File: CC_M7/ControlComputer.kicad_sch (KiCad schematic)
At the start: 41 parts, among them J1 1x03_BootPin, U1 STM32H743VITx, Y1 25MHz

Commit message: update
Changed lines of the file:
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@@
 	(wire
 		(pts
-			(xy 104.14 140.97) (xy 113.03 140.97)
+			(xy 104.14 140.97) (xy 118.11 140.97)
 		)
 		(stroke
@@
 	(global_label "ADC1"
 		(shape input)
-		(at 113.03 140.97 0)
-		(fields_autoplaced yes)
-		(effects
-			(font
-				(size 1.27 1.27)
-			)
-			(justify left)
-		)
-		(property "Intersheetrefs" "${INTERSHEET_REFS}"
-			(at 120.8533 140.97 0)
-			(effects
-				(font
+		(at 118.11 140.97 0)
+		(fields_autoplaced yes)
+		(effects
+			(font
+				(size 1.27 1.27)
+			)
+			(justify left)
+		)
+		(property "Intersheetrefs" "${INTERSHEET_REFS}"
+			(at 125.9333 140.97 0)
+			(effects
+				(font

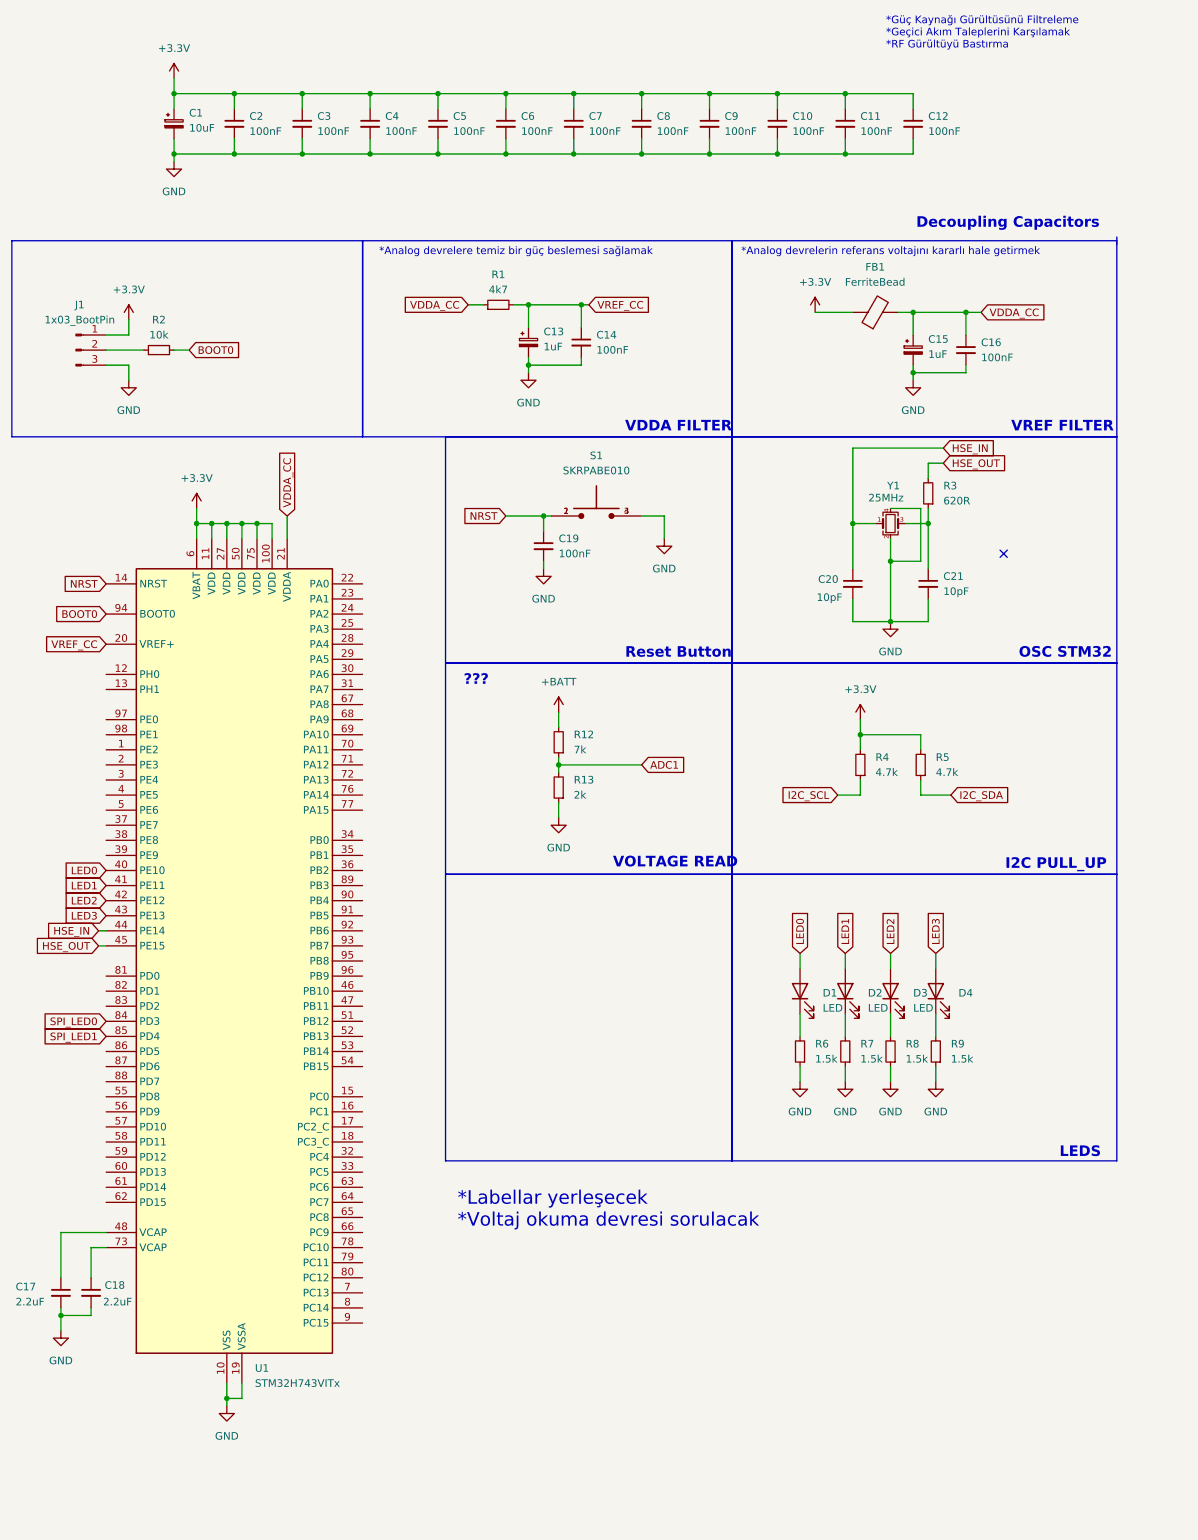
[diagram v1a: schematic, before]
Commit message: STM32H743VIT6 labels updated
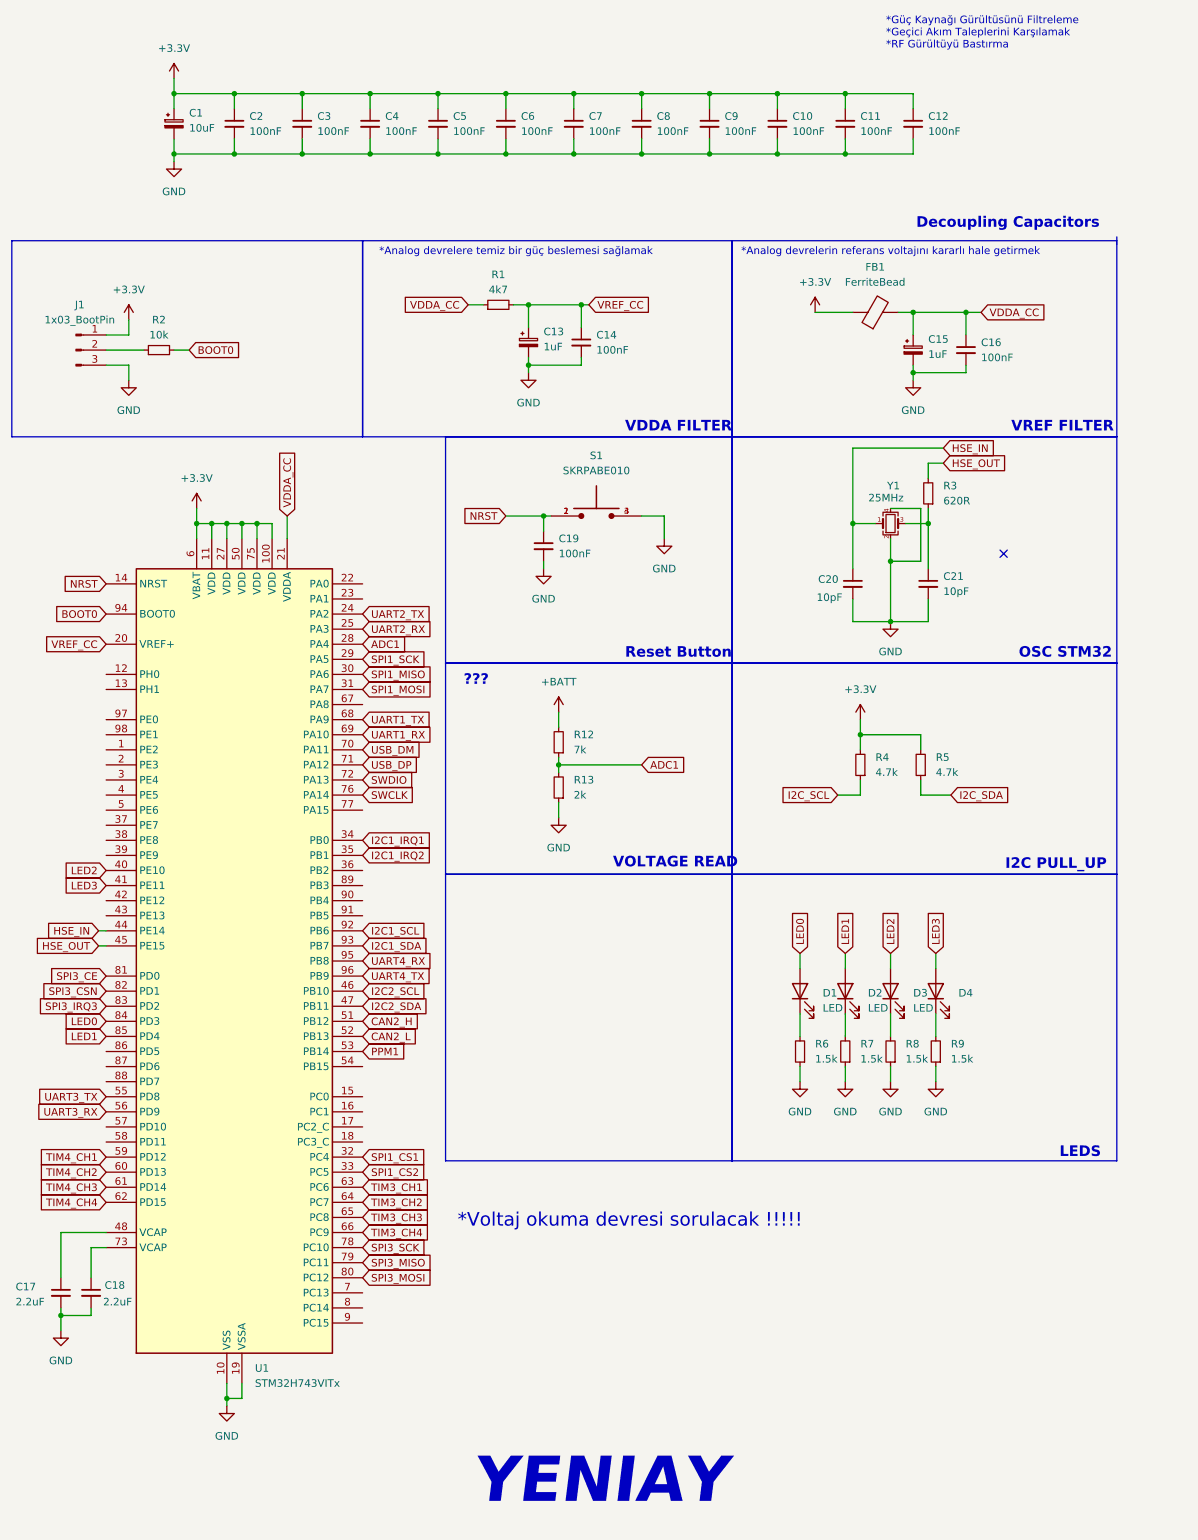
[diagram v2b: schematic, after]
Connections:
- net  SPI_LED0 is gone; now on net LED0: U1.84 (PD3)
- net SPI_LED1 is gone; now on net LED1: U1.85 (PD4)
- net ADC1: now also U1.28 (PA4)
- net LED0: no longer U1.40 (PE10)
- net LED1: no longer U1.41 (PE11)
- net LED2: now also U1.40 (PE10); no longer U1.42 (PE12)
- net LED3: now also U1.41 (PE11); no longer U1.43 (PE13)
- net UART2_TX: now reaches U1.24 (PA2)
- net UART2_RX: now reaches U1.25 (PA3)
- net SPI1_SCK: now reaches U1.29 (PA5)
- net SPI1_MISO: now reaches U1.30 (PA6)
- net SPI1_MOSI: now reaches U1.31 (PA7)
- net SPI1_CS1: now reaches U1.32 (PC4)
- net SPI1_CS2: now reaches U1.33 (PC5)
- net I2C1_IRQ1: now reaches U1.34 (PB0)
- net I2C1_IRQ2: now reaches U1.35 (PB1)
- net I2C2_SCL: now reaches U1.46 (PB10)
- net I2C2_SDA: now reaches U1.47 (PB11)
- net CAN2_H: now reaches U1.51 (PB12)
- net CAN2_L: now reaches U1.52 (PB13)
- net PPM1: now reaches U1.53 (PB14)
- net UART3_TX : now reaches U1.55 (PD8)
- net UART3_RX: now reaches U1.56 (PD9)
- net TIM4_CH1: now reaches U1.59 (PD12)
- net TIM4_CH2: now reaches U1.60 (PD13)
- net TIM4_CH3: now reaches U1.61 (PD14)
- net TIM4_CH4: now reaches U1.62 (PD15)
- net TIM3_CH1: now reaches U1.63 (PC6)
- net TIM3_CH2: now reaches U1.64 (PC7)
- net TIM3_CH3: now reaches U1.65 (PC8)
- net TIM3_CH4: now reaches U1.66 (PC9)
- net UART1_TX: now reaches U1.68 (PA9)
- net UART1_RX: now reaches U1.69 (PA10)
- net USB_DM: now reaches U1.70 (PA11)
- net USB_DP: now reaches U1.71 (PA12)
- net SWDIO: now reaches U1.72 (PA13)
- net SWCLK: now reaches U1.76 (PA14)
- net SPI3_SCK: now reaches U1.78 (PC10)
- net SPI3_MISO: now reaches U1.79 (PC11)
- net SPI3_MOSI: now reaches U1.80 (PC12)
- net SPI3_CE: now reaches U1.81 (PD0)
- net SPI3_CSN: now reaches U1.82 (PD1)
- net SPI3_IRQ3: now reaches U1.83 (PD2)
- net I2C1_SCL: now reaches U1.92 (PB6)
- net I2C1_SDA : now reaches U1.93 (PB7)
- net UART4_RX: now reaches U1.95 (PB8)
- net UART4_TX: now reaches U1.96 (PB9)
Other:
- note added: "*Voltaj okuma devresi sorulacak !!!!!"
- note added: "YENIAY"
- note removed: "*Labellar yerleşecek *Voltaj okuma devresi sorulacak"
- company: YENIAY -> (none)

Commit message: label control
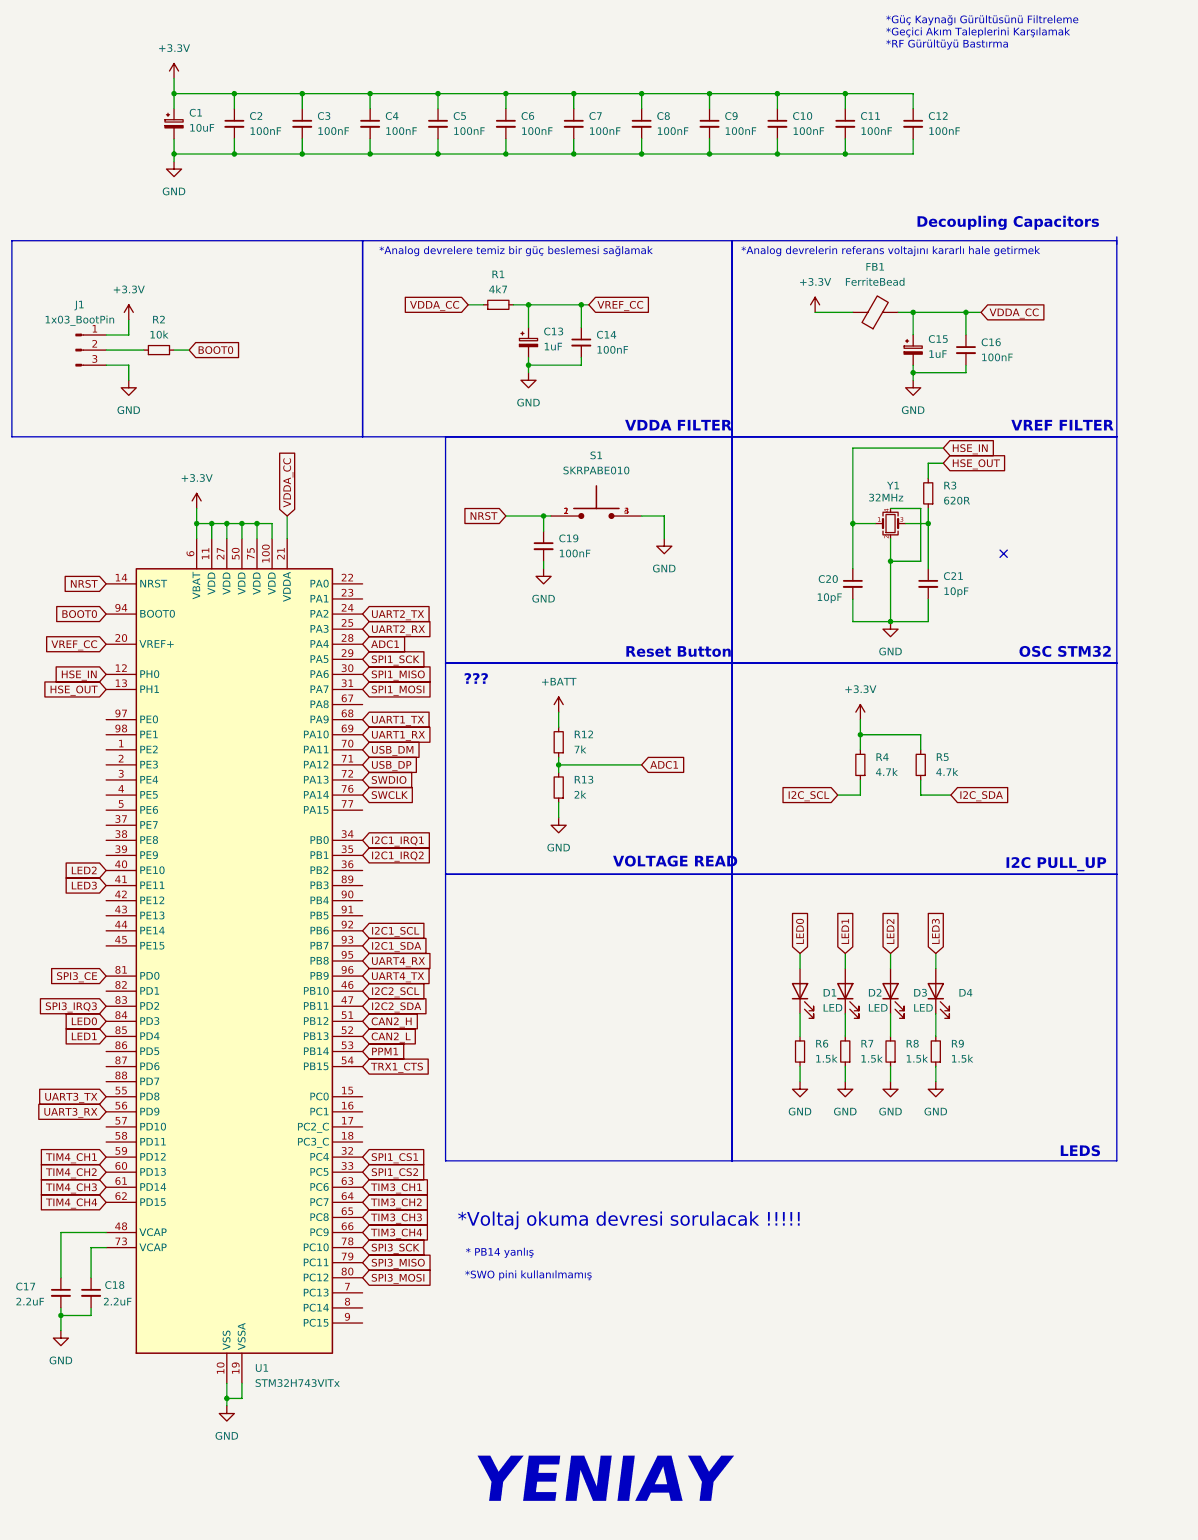
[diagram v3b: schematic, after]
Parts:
- Y1: value 25MHz -> 32MHz
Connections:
- net HSE_IN: now also U1.12 (PH0); no longer U1.44 (PE14)
- net HSE_OUT: now also U1.13 (PH1); no longer U1.45 (PE15)
- net TRX1_CTS: now reaches U1.54 (PB15)
- net SPI3_CSN: no longer names the net of U1.82 (PD1)
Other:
- note added: "* PB14 yanlış"
- note added: "*SWO pini kullanılmamış"
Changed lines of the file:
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@@
 	(wire
 		(pts
-			(xy 26.67 168.91) (xy 27.94 168.91)
-		)
-		(stroke
-			(width 0)
-			(type default)
-		)
-	)
-	(wire
-		(pts
 			(xy 104.14 140.97) (xy 104.14 142.24)
 		)
@@
 	(wire
 		(pts
-			(xy 26.67 171.45) (xy 27.94 171.45)
-		)
-		(stroke
-			(width 0)
-			(type default)
-		)
-	)
-	(wire
-		(pts
 			(xy 27.94 219.71) (xy 20.32 219.71)
 		)
@@
 		)
 	)
+	(text "*SWO pini kullanılmamış"
+		(exclude_from_sim no)
+		(at 99.06 227.076 0)
+		(effects
+			(font
+				(size 1.27 1.27)
+			)
+		)
+	)
 	(text "OSC STM32"
 		(exclude_from_sim no)
@@
 		)
 	)
+	(text "* PB14 yanlış"
+		(exclude_from_sim no)
+		(at 94.234 223.266 0)
+		(effects
+			(font
+				(size 1.27 1.27)
+			)
+		)
+	)
 	(text "???"
 		(exclude_from_sim no)
@@
 	(global_label "HSE_IN"
 		(shape input)
-		(at 26.67 168.91 180)
+		(at 27.94 125.73 180)
 		(fields_autoplaced yes)
 		(effects
@@
 		)
 		(property "Intersheetrefs" "${INTERSHEET_REFS}"
-			(at 17.0929 168.91 0)
+			(at 18.3629 125.73 0)
 			(effects
 				(font
@@
 		)
 	)
-	(global_label "SPI3_CSN"
-		(shape input)
-		(at 27.94 179.07 180)
-		(fields_autoplaced yes)
-		(effects
-			(font
-				(size 1.27 1.27)
-			)
-			(justify right)
-		)
-		(property "Intersheetrefs" "${INTERSHEET_REFS}"
-			(at 15.8834 179.07 0)
-			(effects
-				(font
-					(size 1.27 1.27)
-				)
-				(justify right)
-				(hide yes)
-			)
-		)
-	)
 	(global_label "BOOT0"
 		(shape input)
@@
 		)
 	)
+	(global_label "TRX1_CTS"
+		(shape input)
+		(at 71.12 191.77 0)
+		(fields_autoplaced yes)
+		(effects
+			(font
+				(size 1.27 1.27)
+			)
+			(justify left)
+		)
+		(property "Intersheetrefs" "${INTERSHEET_REFS}"
+			(at 83.1765 191.77 0)
+			(effects
+				(font
+					(size 1.27 1.27)
+				)
+				(justify left)
+				(hide yes)
+			)
+		)
+	)
 	(global_label "SPI3_SCK"
 		(shape input)
@@
 	(global_label "HSE_OUT"
 		(shape input)
-		(at 26.67 171.45 180)
+		(at 27.94 128.27 180)
 		(fields_autoplaced yes)
 		(effects
@@
 		)
 		(property "Intersheetrefs" "${INTERSHEET_REFS}"
-			(at 15.3996 171.45 0)
+			(at 16.6696 128.27 0)
 			(effects
 				(font
@@
 			)
 		)
-		(property "Value" "25MHz"
+		(property "Value" "32MHz"
 			(at 159.258 96.012 0)
 			(effects

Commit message: Control board updated
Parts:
- removed R12: 7k, symbol Device:R_Small
- removed R13: 2k, symbol Device:R_Small
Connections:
- net SPI3_IRQ: now reaches U1.82 (PD1)
- net SWO: now reaches U1.89 (PB3)
- net CAN2_H renamed CAN2_RX
- net CAN2_L renamed CAN2_TX
- net PPM1 renamed TRX1_RTS
- net SPI3_CE renamed SPI3_CS
- net SPI3_IRQ3: no longer names the net of U1.83 (PD2)
- net UART3_TX  renamed UART3_TX
- no-connect marks 1 -> 0
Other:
- note removed: "*Voltaj okuma devresi sorulacak !!!!!"
- note removed: "???"
- note removed: "VOLTAGE READ"
- moved on the sheet: J1, R2, R4, R5

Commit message: Connectors updated
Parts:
- C20, C21: value 10pF -> 12pF
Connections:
- net I2C_SCL is gone; now on net I2C1_SCL: R4.1
- net I2C1_IRQ1: now also U1.44 (PE14); no longer U1.34 (PB0)
- net I2C1_IRQ2: now also U1.45 (PE15); no longer U1.35 (PB1)
- net PPM1: now reaches U1.22 (PA0)
- net ADC1: no longer names the net of U1.28 (PA4)
- net I2C_SDA renamed I2C1_SDA
- net TIM4_CH1: no longer names the net of U1.59 (PD12)
- net TIM4_CH2: no longer names the net of U1.60 (PD13)
- new net ADC1_VS: U1.34 (PB0)
- new net ADC2_AS: U1.35 (PB1)

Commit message: nrf
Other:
- moved on the sheet: D1, D2, D3, D4, R6, R7, R8, R9

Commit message: final schematic 6 warning
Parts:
- removed J1: 1x03_BootPin, symbol Connector:Conn_01x03_Pin
- removed R2: 10k, symbol Device:R_Small
- added JP1, JP2, JP3, JP4: SWDIO, symbol Jumper:Jumper_2_Bridged
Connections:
- net I2C1_SDA  is gone; now on net I2C1_SDA: U1.93 (PB7)
- net NRST: now also JP4.1 (A)
- net SWCLK: now also JP2.1 (A)
- net SWDIO: now also JP3.1 (A)
- net SWO: now also JP1.1 (A)
- net PE2: now reaches U1.1 (PE2)
- net PE3: now reaches U1.2 (PE3)
- net PA1: now reaches U1.23 (PA1)
- net PA4: now reaches U1.28 (PA4)
- net PE4: now reaches U1.3 (PE4)
- net PE5: now reaches U1.4 (PE5)
- net PE6: now reaches U1.5 (PE6)
- net PC13: now reaches U1.7 (PC13)
- net PC14: now reaches U1.8 (PC14)
- net PC15: now reaches U1.9 (PC15)
- net BOOT0: no longer names the net of U1.94 (BOOT0)
- net PPM1 renamed PA0
- new net J2_32: JP1.2 (B)
- new net J2_36: JP2.2 (B)
- new net J2_38: JP3.2 (B)
- new net J2_40: JP4.2 (B)
- no-connect marks 0 -> 25
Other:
- note added: "DECOUPLING"
- note added: "RESET"
- note removed: "* PB14 yanlış"
- note removed: "*SWO pini kullanılmamış"
- note removed: "Decoupling Capacitors"
- note removed: "Reset Button"
- moved on the sheet: C17, C18, C19, C21, D1, D2, D3, D4, R4, R5, R6, R7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

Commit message: Changes updated @ CCM7.docx
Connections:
- net ADC1_VS: no longer names the net of U1.34 (PB0)
- net ADC2_AS: no longer names the net of U1.35 (PB1)
- net TRX1_CTS: no longer names the net of U1.54 (PB15)
- net TRX1_RTS: no longer names the net of U1.53 (PB14)
- no-connect marks 25 -> 29
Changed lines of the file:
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@@
 	)
 	(no_connect
+		(at 87.63 190.5)
+	)
+	(no_connect
 		(at 87.63 205.74)
 	)
 	(no_connect
+		(at 87.63 193.04)
+	)
+	(no_connect
 		(at 87.63 203.2)
 	)
@@
 	)
 	(no_connect
+		(at 87.63 157.48)
+	)
+	(no_connect
 		(at 44.45 208.28)
 	)
@@
 	)
 	(no_connect
+		(at 87.63 154.94)
+	)
+	(no_connect
 		(at 44.45 134.62)
 	)
@@
 		)
 	)
-	(global_label "ADC1_VS"
-		(shape input)
-		(at 87.63 154.94 0)
-		(fields_autoplaced yes)
-		(effects
-			(font
-				(size 1.27 1.27)
-			)
-			(justify left)
-		)
-		(property "Intersheetrefs" "${INTERSHEET_REFS}"
-			(at 98.719 154.94 0)
-			(effects
-				(font
-					(size 1.27 1.27)
-				)
-				(justify left)
-				(hide yes)
-			)
-		)
-	)
 	(global_label "TIM4_CH3"
 		(shape input)
@@
 		)
 	)
-	(global_label "ADC2_AS"
-		(shape input)
-		(at 87.63 157.48 0)
-		(fields_autoplaced yes)
-		(effects
-			(font
-				(size 1.27 1.27)
-			)
-			(justify left)
-		)
-		(property "Intersheetrefs" "${INTERSHEET_REFS}"
-			(at 98.719 157.48 0)
-			(effects
-				(font
-					(size 1.27 1.27)
-				)
-				(justify left)
-				(hide yes)
-			)
-		)
-	)
 	(global_label "SPI1_MOSI"
 		(shape input)
@@
 		)
 	)
-	(global_label "TRX1_CTS"
-		(shape input)
-		(at 87.63 193.04 0)
-		(fields_autoplaced yes)
-		(effects
-			(font
-				(size 1.27 1.27)
-			)
-			(justify left)
-		)
-		(property "Intersheetrefs" "${INTERSHEET_REFS}"
-			(at 99.6865 193.04 0)
-			(effects
-				(font
-					(size 1.27 1.27)
-				)
-				(justify left)
-				(hide yes)
-			)
-		)
-	)
 	(global_label "SPI3_SCK"
 		(shape input)
@@
 			(effects
 				(font
-					(size 1.27 1.27)
-				)
-				(justify left)
-				(hide yes)
-			)
-		)
-	)
-	(global_label "TRX1_RTS"
-		(shape input)
-		(at 87.63 190.5 0)
-		(fields_autoplaced yes)
-		(effects
-			(font
-				(size 1.27 1.27)
-			)
-			(justify left)
-		)
-		(property "Intersheetrefs" "${INTERSHEET_REFS}"
-			(at 99.6865 190.5 0)
-			(effects
-				(font
